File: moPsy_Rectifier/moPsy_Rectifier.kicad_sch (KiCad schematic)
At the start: 41 parts, among them J1 Conn_01x01_Male, J10 Conn_01x01_Male, J11 Conn_01x01_Male, J12 Conn_01x03_Male, J13 Conn_01x08_Male, J14 Conn_01x01_Male, J15 Conn_01x01_Male, J16 Conn_01x01_Male, J17 Conn_01x01_Male, J2 Conn_01x01_Male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

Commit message: PCB Layout
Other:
- moved on the sheet: J6
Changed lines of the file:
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@@
     (stroke (width 0) (type default) (color 0 0 0 0))
   )
-  (wire (pts (xy 58.42 105.41) (xy 35.56 105.41))
+  (wire (pts (xy 77.47 105.41) (xy 71.12 105.41))
     (stroke (width 0) (type default) (color 0 0 0 0))
   )
@@
     (stroke (width 0) (type default) (color 0 0 0 0))
   )
-  (wire (pts (xy 71.12 105.41) (xy 77.47 105.41))
-    (stroke (width 0) (type default) (color 0 0 0 0))
-  )
   (wire (pts (xy 72.39 85.09) (xy 72.39 87.63))
     (stroke (width 0) (type default) (color 0 0 0 0))
@@
   )
   (wire (pts (xy 236.22 31.75) (xy 229.87 31.75))
+    (stroke (width 0) (type default) (color 0 0 0 0))
+  )
+  (wire (pts (xy 55.88 105.41) (xy 35.56 105.41))
     (stroke (width 0) (type default) (color 0 0 0 0))
   )
@@
     (pin "1")
   )
-  (symbol (lib_id "Connector:Conn_01x01_Male") (at 63.5 105.41 180) (unit 1)
-    (in_bom yes) (on_board yes)
-    (property "Reference" "J6" (id 0) (at 60.96 106.68 0))
-    (property "Value" "Conn_01x01_Male" (id 1) (at 55.88 102.87 0))
-    (property "Footprint" "moPsy:Connector FS-P475" (id 2) (at 63.5 105.41 0)
-      (effects (font (size 1.27 1.27)) hide)
-    )
-    (property "Datasheet" "~" (id 3) (at 63.5 105.41 0)
+  (symbol (lib_id "Connector:Conn_01x01_Male") (at 60.96 105.41 180) (unit 1)
+    (in_bom yes) (on_board yes)
+    (property "Reference" "J6" (id 0) (at 58.42 106.68 0))
+    (property "Value" "Conn_01x01_Male" (id 1) (at 53.34 102.87 0))
+    (property "Footprint" "moPsy:Connector FS-P475" (id 2) (at 60.96 105.41 0)
+      (effects (font (size 1.27 1.27)) hide)
+    )
+    (property "Datasheet" "~" (id 3) (at 60.96 105.41 0)
       (effects (font (size 1.27 1.27)) hide)
     )
@@
   (symbol (lib_id "Connector:Conn_01x01_Male") (at 66.04 105.41 0) (unit 1)
     (in_bom yes) (on_board yes)
-    (property "Reference" "J9" (id 0) (at 67.31 104.14 0))
+    (property "Reference" "J9" (id 0) (at 67.31 102.87 0))
     (property "Value" "Conn_01x01_Male" (id 1) (at 68.58 107.95 0))
     (property "Footprint" "moPsy:Connector FS-P475" (id 2) (at 66.04 105.41 0)

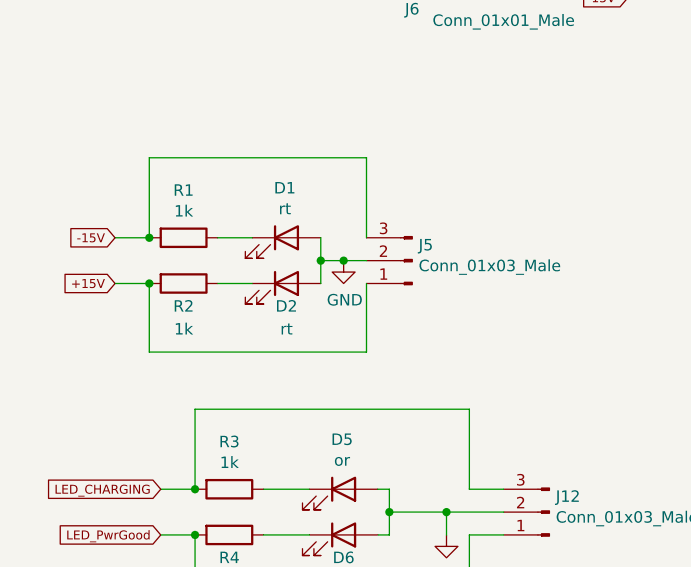
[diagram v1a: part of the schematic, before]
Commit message: Fix direction of V+ Pwr indicator LED
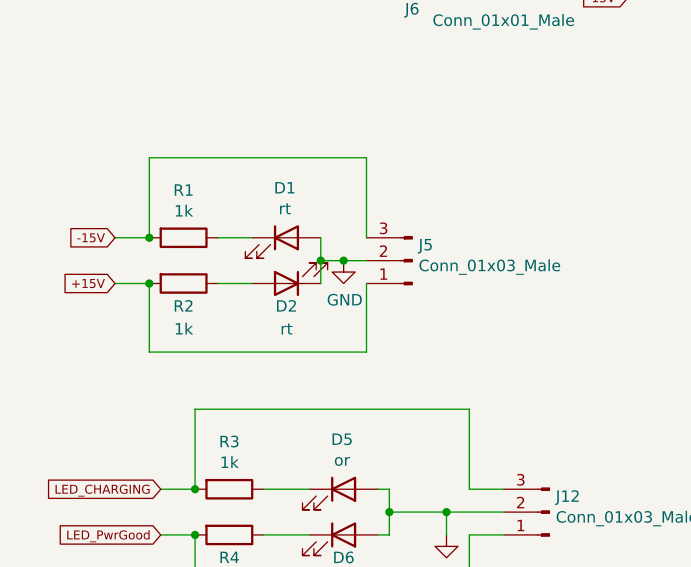
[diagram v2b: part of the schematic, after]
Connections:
- net GND: now also D2.1 (K); no longer D2.2 (A)
- net at R2.1: now also D2.2 (A); no longer D2.1 (K)
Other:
- moved on the sheet: D2
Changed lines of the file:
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@@
     (pin "2")
   )
-  (symbol (lib_id "Device:LED") (at 44.45 137.16 0) (unit 1)
+  (symbol (lib_id "Device:LED") (at 44.45 137.16 180) (unit 1)
     (in_bom yes) (on_board yes)
     (property "Reference" "D2" (id 0) (at 44.45 139.7 0))
